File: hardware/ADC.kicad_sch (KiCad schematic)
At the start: 22 parts

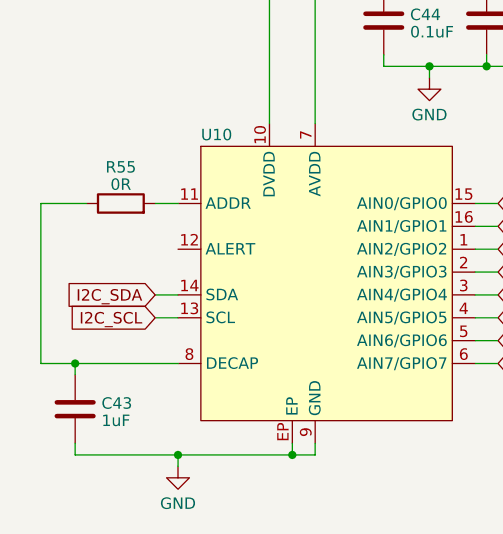
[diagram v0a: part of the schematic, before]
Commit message: working on hardware agin as well as implimentded auto adc init and read
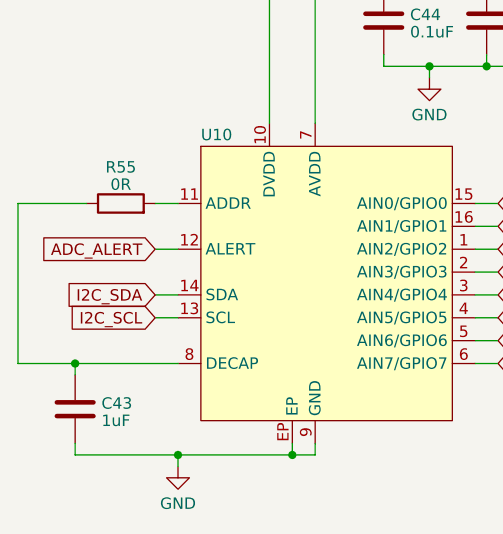
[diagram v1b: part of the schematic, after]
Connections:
- net ADC_ALERT: now reaches U10.12 (ALERT)
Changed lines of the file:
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@@
     (stroke (width 0) (type default))
   )
-  (wire (pts (xy 40.64 101.6) (xy 44.45 101.6))
+  (wire (pts (xy 38.1 101.6) (xy 44.45 101.6))
     (stroke (width 0) (type default))
   )
@@
     (stroke (width 0) (type default))
   )
-  (wire (pts (xy 40.64 83.82) (xy 40.64 101.6))
+  (wire (pts (xy 38.1 83.82) (xy 38.1 101.6))
     (stroke (width 0) (type default))
   )
@@
     (stroke (width 0) (type default))
   )
+  (wire (pts (xy 53.34 88.9) (xy 55.88 88.9))
+    (stroke (width 0) (type default))
+  )
   (wire (pts (xy 44.45 101.6) (xy 44.45 102.87))
     (stroke (width 0) (type default))
@@
     (stroke (width 0) (type default))
   )
-  (wire (pts (xy 45.72 83.82) (xy 40.64 83.82))
+  (wire (pts (xy 38.1 83.82) (xy 45.72 83.82))
     (stroke (width 0) (type default))
   )
@@
     )
   )
+  (global_label "ADC_ALERT" (shape input) (at 53.34 88.9 180) (fields_autoplaced)
+    (effects (font (size 1.27 1.27)) (justify right))
+    (property "Intersheetrefs" "${INTERSHEET_REFS}" (at 40.3347 88.9 0)
+      (effects (font (size 1.27 1.27)) (justify right) hide)
+    )
+  )

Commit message: working on hardware
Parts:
- C49: renamed from C43; footprint (none) -> Capacitor_SMD:C_0603_1608Metric
- C50: renamed from C44; footprint (none) -> Capacitor_SMD:C_0603_1608Metric
- C51: renamed from C46; footprint (none) -> Capacitor_SMD:C_0603_1608Metric
- C52: renamed from C45; footprint (none) -> Capacitor_SMD:C_0603_1608Metric
- renumbered R55 to R62, R58 to R63, R59 to R64, R60 to R65, R61 to R66, R62 to R67, R63 to R68, R64 to R69, R65 to R70, R66 to R71, R67 to R72, R68 to R73, R69 to R74, R70 to R75, R71 to R76, R72 to R77, R73 to R78, U10 to U12
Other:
- note added: "DEVIDER NETWORKS FOR ADC INPUT"
- note added: "I2C ADC"

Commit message: working assighning footprints still
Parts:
- R62, R63, R64, R65, R66, R67, R68, R69, R70, R71, R72, R73, R74, R75, R76, R77, R78: footprint (none) -> Resistor_SMD:R_0603_1608Metric
- U12: footprint (none) -> Package_DFN_QFN:WQFN-16-1EP_3x3mm_P0.5mm_EP1.6x1.6mm_ThermalVias
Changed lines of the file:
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@@
       (effects (font (size 1.27 1.27)) (justify left))
     )
-    (property "Footprint" "" (at 162.052 82.55 90)
+    (property "Footprint" "Resistor_SMD:R_0603_1608Metric" (at 162.052 82.55 90)
       (effects (font (size 1.27 1.27)) hide)
     )
@@
       (effects (font (size 1.27 1.27)))
     )
-    (property "Footprint" "" (at 59.69 76.2 0)
+    (property "Footprint" "Package_DFN_QFN:WQFN-16-1EP_3x3mm_P0.5mm_EP1.6x1.6mm_ThermalVias" (at 59.69 76.2 0)
       (effects (font (size 1.27 1.27)) hide)
     )
@@
       (effects (font (size 1.27 1.27)) (justify left))
     )
-    (property "Footprint" "" (at 162.052 92.71 90)
+    (property "Footprint" "Resistor_SMD:R_0603_1608Metric" (at 162.052 92.71 90)
       (effects (font (size 1.27 1.27)) hide)
     )
@@
       (effects (font (size 1.27 1.27)) (justify left))
     )
-    (property "Footprint" "" (at 187.452 82.55 90)
+    (property "Footprint" "Resistor_SMD:R_0603_1608Metric" (at 187.452 82.55 90)
       (effects (font (size 1.27 1.27)) hide)
     )
@@
       (effects (font (size 1.27 1.27)) (justify left))
     )
-    (property "Footprint" "" (at 187.452 92.71 90)
+    (property "Footprint" "Resistor_SMD:R_0603_1608Metric" (at 187.452 92.71 90)
       (effects (font (size 1.27 1.27)) hide)
     )
@@
       (effects (font (size 1.27 1.27)) (justify left))
     )
-    (property "Footprint" "" (at 235.712 92.71 90)
+    (property "Footprint" "Resistor_SMD:R_0603_1608Metric" (at 235.712 92.71 90)
       (effects (font (size 1.27 1.27)) hide)
     )
@@
       (effects (font (size 1.27 1.27)) (justify left))
     )
-    (property "Footprint" "" (at 200.152 82.55 90)
+    (property "Footprint" "Resistor_SMD:R_0603_1608Metric" (at 200.152 82.55 90)
       (effects (font (size 1.27 1.27)) hide)
     )
@@
       (effects (font (size 1.27 1.27)) (justify left))
     )
-    (property "Footprint" "" (at 248.412 82.55 90)
+    (property "Footprint" "Resistor_SMD:R_0603_1608Metric" (at 248.412 82.55 90)
       (effects (font (size 1.27 1.27)) hide)
     )
@@
       (effects (font (size 1.27 1.27)) (justify left))
     )
-    (property "Footprint" "" (at 174.752 82.55 90)
+    (property "Footprint" "Resistor_SMD:R_0603_1608Metric" (at 174.752 82.55 90)
       (effects (font (size 1.27 1.27)) hide)
     )
@@
       (effects (font (size 1.27 1.27)) (justify left))
     )
-    (property "Footprint" "" (at 224.282 82.55 90)
+    (property "Footprint" "Resistor_SMD:R_0603_1608Metric" (at 224.282 82.55 90)
       (effects (font (size 1.27 1.27)) hide)
     )
@@
       (effects (font (size 1.27 1.27)) (justify left))
     )
-    (property "Footprint" "" (at 224.282 92.71 90)
+    (property "Footprint" "Resistor_SMD:R_0603_1608Metric" (at 224.282 92.71 90)
       (effects (font (size 1.27 1.27)) hide)
     )
@@
       (effects (font (size 1.27 1.27)) (justify left))
     )
-    (property "Footprint" "" (at 211.582 82.55 90)
+    (property "Footprint" "Resistor_SMD:R_0603_1608Metric" (at 211.582 82.55 90)
       (effects (font (size 1.27 1.27)) hide)
     )
@@
       (effects (font (size 1.27 1.27)))
     )
-    (property "Footprint" "" (at 49.53 85.598 90)
+    (property "Footprint" "Resistor_SMD:R_0603_1608Metric" (at 49.53 85.598 90)
       (effects (font (size 1.27 1.27)) hide)
     )
@@
       (effects (font (size 1.27 1.27)) (justify left))
     )
-    (property "Footprint" "" (at 211.582 92.71 90)
+    (property "Footprint" "Resistor_SMD:R_0603_1608Metric" (at 211.582 92.71 90)
       (effects (font (size 1.27 1.27)) hide)
     )
@@
       (effects (font (size 1.27 1.27)) (justify left))
     )
-    (property "Footprint" "" (at 248.412 92.71 90)
+    (property "Footprint" "Resistor_SMD:R_0603_1608Metric" (at 248.412 92.71 90)
       (effects (font (size 1.27 1.27)) hide)
     )
@@
       (effects (font (size 1.27 1.27)) (justify left))
     )
-    (property "Footprint" "" (at 235.712 82.55 90)
+    (property "Footprint" "Resistor_SMD:R_0603_1608Metric" (at 235.712 82.55 90)
       (effects (font (size 1.27 1.27)) hide)
     )
@@
       (effects (font (size 1.27 1.27)) (justify left))
     )
-    (property "Footprint" "" (at 200.152 92.71 90)
+    (property "Footprint" "Resistor_SMD:R_0603_1608Metric" (at 200.152 92.71 90)
       (effects (font (size 1.27 1.27)) hide)
     )
@@
       (effects (font (size 1.27 1.27)) (justify left))
     )
-    (property "Footprint" "" (at 174.752 92.71 90)
-      (effects (font (size 1.27 1.27)) hide)
-    )
+    (property "Footprint" "Resistor_SMD:R_0603_1608Metric" (at 174.752 92.71 90)
+      (effects (font (size 1.27 1.27)) hide)
+    )

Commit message: coldent sleep so came back and did somre routing
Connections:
- net GND: now also U12.17 (EP); no longer U12.EP
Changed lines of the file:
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@@
     (pin "15")
     (pin "16")
+    (pin "17")
     (pin "2")
     (pin "3")
@@
     (pin "8")
     (pin "9")
-    (pin "EP")
     (instances
       (project "usbc-car-module"

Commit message: working on routing still  finnished psu section
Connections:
- net B_USB-C_BUCK_OUT: now also R71.1; no longer R75.1
- net B_USB-C_BUCK_OUT_ADC: now also R71.2, R72.1, U12.3 (AIN4/GPIO4); no longer R75.2, R76.1, U12.5 (AIN6/GPIO6)
- net B_USB-C_CSN: now also R73.1; no longer R77.1
- net B_USB-C_CSN_ADC: now also R73.2, R74.1, U12.4 (AIN5/GPIO5); no longer R77.2, R78.1, U12.6 (AIN7/GPIO7)
- net F_USB-C_BUCK_OUT: now also R75.1; no longer R71.1
- net F_USB-C_BUCK_OUT_ADC: now also R75.2, R76.1, U12.5 (AIN6/GPIO6); no longer R71.2, R72.1, U12.3 (AIN4/GPIO4)
- net F_USB-C_CSN: now also R77.1; no longer R73.1
- net F_USB-C_CSN_ADC: now also R77.2, R78.1, U12.6 (AIN7/GPIO7); no longer R73.2, R74.1, U12.4 (AIN5/GPIO5)
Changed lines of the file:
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@@
     (effects (font (size 1.27 1.27)) (justify left bottom))
   )
-  (global_label "B_USB-C_CSN_ADC" (shape input) (at 91.44 101.6 0) (fields_autoplaced)
+  (global_label "F_USB-C_CSN_ADC" (shape input) (at 91.44 101.6 0) (fields_autoplaced)
     (effects (font (size 1.27 1.27)) (justify left))
     (property "Intersheetrefs" "${INTERSHEET_REFS}" (at 112.6096 101.6 0)
@@
     )
   )
-  (global_label "B_USB-C_BUCK_OUT_ADC" (shape input) (at 233.68 86.36 90) (fields_autoplaced)
+  (global_label "F_USB-C_BUCK_OUT_ADC" (shape input) (at 233.68 86.36 90) (fields_autoplaced)
     (effects (font (size 1.27 1.27)) (justify left))
     (property "Intersheetrefs" "${INTERSHEET_REFS}" (at 233.68 59.2637 90)
@@
     )
   )
-  (global_label "F_USB-C_BUCK_OUT" (shape input) (at 213.36 76.2 90) (fields_autoplaced)
+  (global_label "B_USB-C_BUCK_OUT" (shape input) (at 213.36 76.2 90) (fields_autoplaced)
     (effects (font (size 1.27 1.27)) (justify left))
     (property "Intersheetrefs" "${INTERSHEET_REFS}" (at 213.36 53.8813 90)
@@
     )
   )
-  (global_label "F_USB-C_BUCK_OUT_ADC" (shape input) (at 209.55 86.36 90) (fields_autoplaced)
+  (global_label "B_USB-C_BUCK_OUT_ADC" (shape input) (at 209.55 86.36 90) (fields_autoplaced)
     (effects (font (size 1.27 1.27)) (justify left))
     (property "Intersheetrefs" "${INTERSHEET_REFS}" (at 209.55 59.4451 90)
@@
     )
   )
-  (global_label "B_USB-C_BUCK_OUT" (shape input) (at 237.49 76.2 90) (fields_autoplaced)
+  (global_label "F_USB-C_BUCK_OUT" (shape input) (at 237.49 76.2 90) (fields_autoplaced)
     (effects (font (size 1.27 1.27)) (justify left))
     (property "Intersheetrefs" "${INTERSHEET_REFS}" (at 237.49 53.6999 90)
@@
     )
   )
-  (global_label "F_USB-C_BUCK_OUT_ADC" (shape input) (at 91.44 93.98 0) (fields_autoplaced)
+  (global_label "B_USB-C_BUCK_OUT_ADC" (shape input) (at 91.44 93.98 0) (fields_autoplaced)
     (effects (font (size 1.27 1.27)) (justify left))
     (property "Intersheetrefs" "${INTERSHEET_REFS}" (at 118.3549 93.98 0)
@@
     )
   )
-  (global_label "B_USB-C_BUCK_OUT_ADC" (shape input) (at 91.44 99.06 0) (fields_autoplaced)
+  (global_label "F_USB-C_BUCK_OUT_ADC" (shape input) (at 91.44 99.06 0) (fields_autoplaced)
     (effects (font (size 1.27 1.27)) (justify left))
     (property "Intersheetrefs" "${INTERSHEET_REFS}" (at 118.5363 99.06 0)
@@
     )
   )
-  (global_label "F_USB-C_CSN_ADC" (shape input) (at 91.44 96.52 0) (fields_autoplaced)
+  (global_label "B_USB-C_CSN_ADC" (shape input) (at 91.44 96.52 0) (fields_autoplaced)
     (effects (font (size 1.27 1.27)) (justify left))
     (property "Intersheetrefs" "${INTERSHEET_REFS}" (at 112.4282 96.52 0)
@@
     )
   )
-  (global_label "B_USB-C_CSN_ADC" (shape input) (at 246.38 86.36 90) (fields_autoplaced)
+  (global_label "F_USB-C_CSN_ADC" (shape input) (at 246.38 86.36 90) (fields_autoplaced)
     (effects (font (size 1.27 1.27)) (justify left))
     (property "Intersheetrefs" "${INTERSHEET_REFS}" (at 246.38 65.1904 90)
@@
     )
   )
-  (global_label "F_USB-C_CSN" (shape input) (at 226.06 76.2 90) (fields_autoplaced)
+  (global_label "B_USB-C_CSN" (shape input) (at 226.06 76.2 90) (fields_autoplaced)
     (effects (font (size 1.27 1.27)) (justify left))
     (property "Intersheetrefs" "${INTERSHEET_REFS}" (at 226.06 59.808 90)
@@
     )
   )
-  (global_label "F_USB-C_CSN_ADC" (shape input) (at 222.25 86.36 90) (fields_autoplaced)
+  (global_label "B_USB-C_CSN_ADC" (shape input) (at 222.25 86.36 90) (fields_autoplaced)
     (effects (font (size 1.27 1.27)) (justify left))
     (property "Intersheetrefs" "${INTERSHEET_REFS}" (at 222.25 65.3718 90)
@@
     )
   )
-  (global_label "B_USB-C_CSN" (shape input) (at 250.19 76.2 90) (fields_autoplaced)
+  (global_label "F_USB-C_CSN" (shape input) (at 250.19 76.2 90) (fields_autoplaced)
     (effects (font (size 1.27 1.27)) (justify left))
     (property "Intersheetrefs" "${INTERSHEET_REFS}" (at 250.19 59.6266 90)

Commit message: finaliseing pcb layout will come back later for a fresh look
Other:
- company: (none) -> MICK MAKE
- title: (none) -> 200W USB PD 3.1 HUB
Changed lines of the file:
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@@
 (kicad_sch (version 20230121) (generator eeschema)
   (paper "A4")
+  (title_block
+    (title "200W USB PD 3.1 HUB")
+    (date "2023-10-03")
+    (rev "A")
+    (company "MICK MAKE")
+    (comment 1 "THIS IS A 2X 100W USB PD SOURCE ")
+    (comment 2 "HUB USB SPEC 3.1")
+    (comment 3 "TOTAL SYSTEM POWER IS ~275w")
+  )
   (junction (at 74.93 57.15) (diameter 0) (color 0 0 0 0)
   )

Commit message: minor revisions
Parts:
- U12: value ~ -> ADS7128
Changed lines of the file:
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@@
       (effects (font (size 1.27 1.27)) (justify left))
     )
-    (property "Value" "~" (at 59.69 76.2 0)
+    (property "Value" "ADS7128 " (at 82.55 76.2 0)
       (effects (font (size 1.27 1.27)))
     )
